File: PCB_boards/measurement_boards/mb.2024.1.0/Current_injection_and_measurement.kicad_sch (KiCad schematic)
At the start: 28 parts, among them J12 Conn_01x08_Socket, J14 Conn_01x02_Socket, J15 Conn_01x08_Socket, J20 shunt +, J21 shunt -, K3 G5LE-1, K4 G5LE-1, K5 G5LE-1, K6 G5LE-1, K7 G5LE-1, Q3 ZVN4206ASTZ, Q4 ZVN4206ASTZ, Q5 ZVN4206ASTZ, Q6 ZVN4206ASTZ, Q7 ZVN4206ASTZ, U5 1085

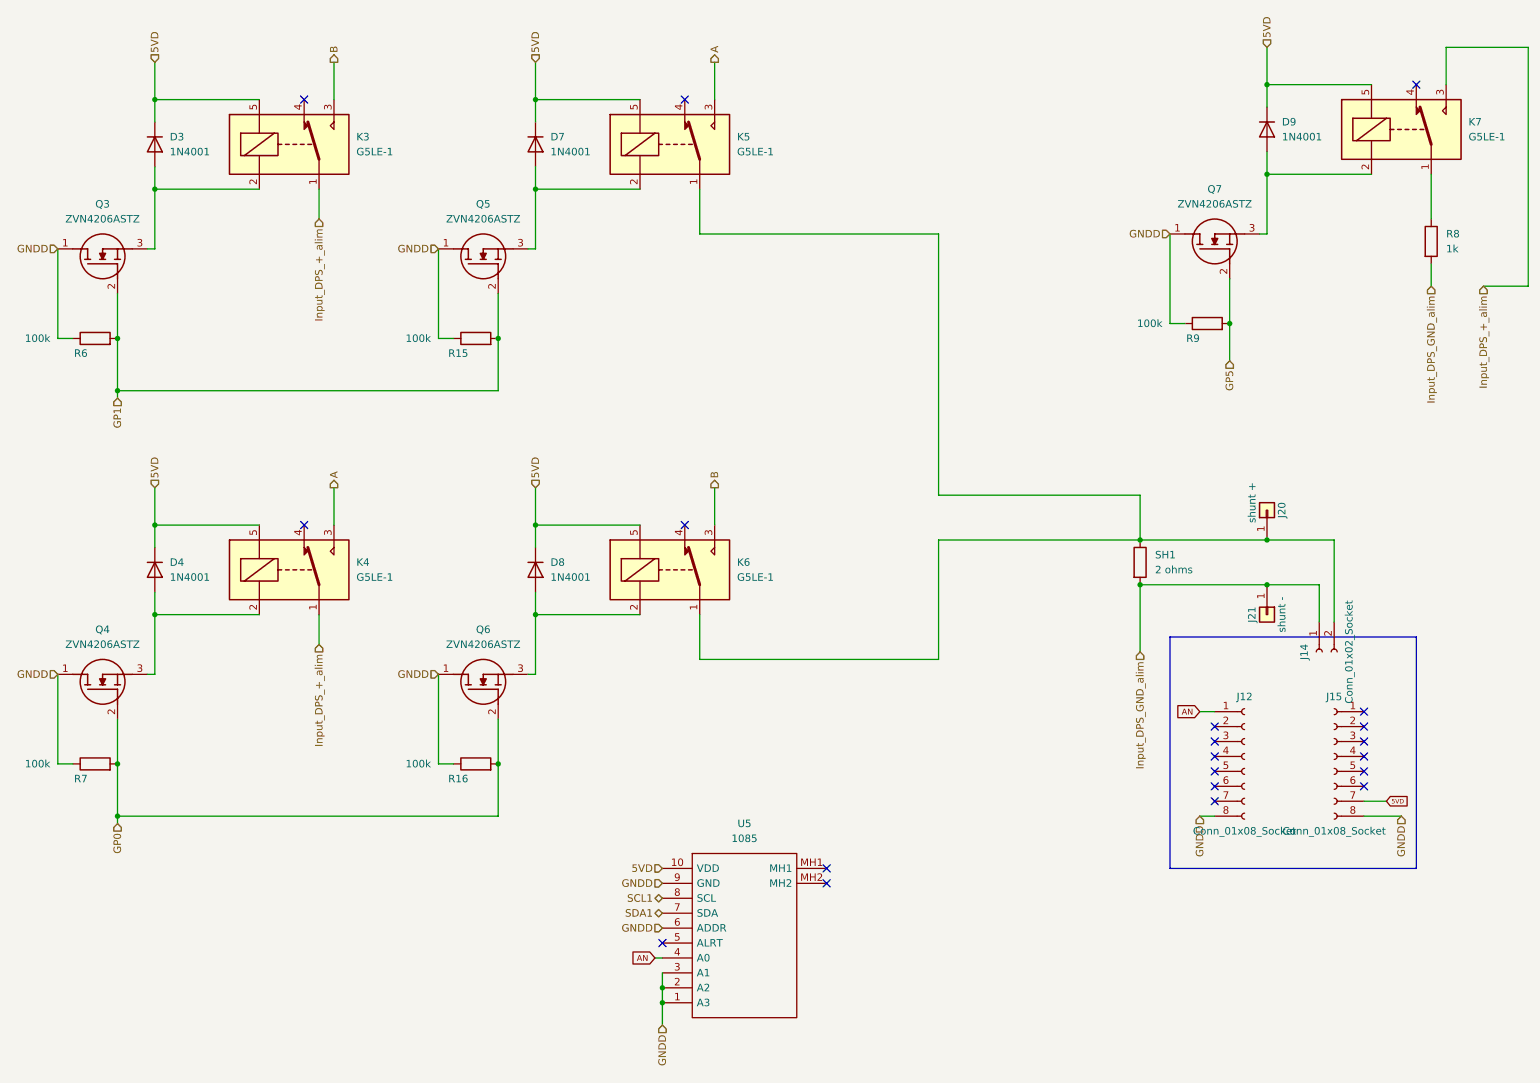
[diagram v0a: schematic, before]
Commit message: update diode 1n4007
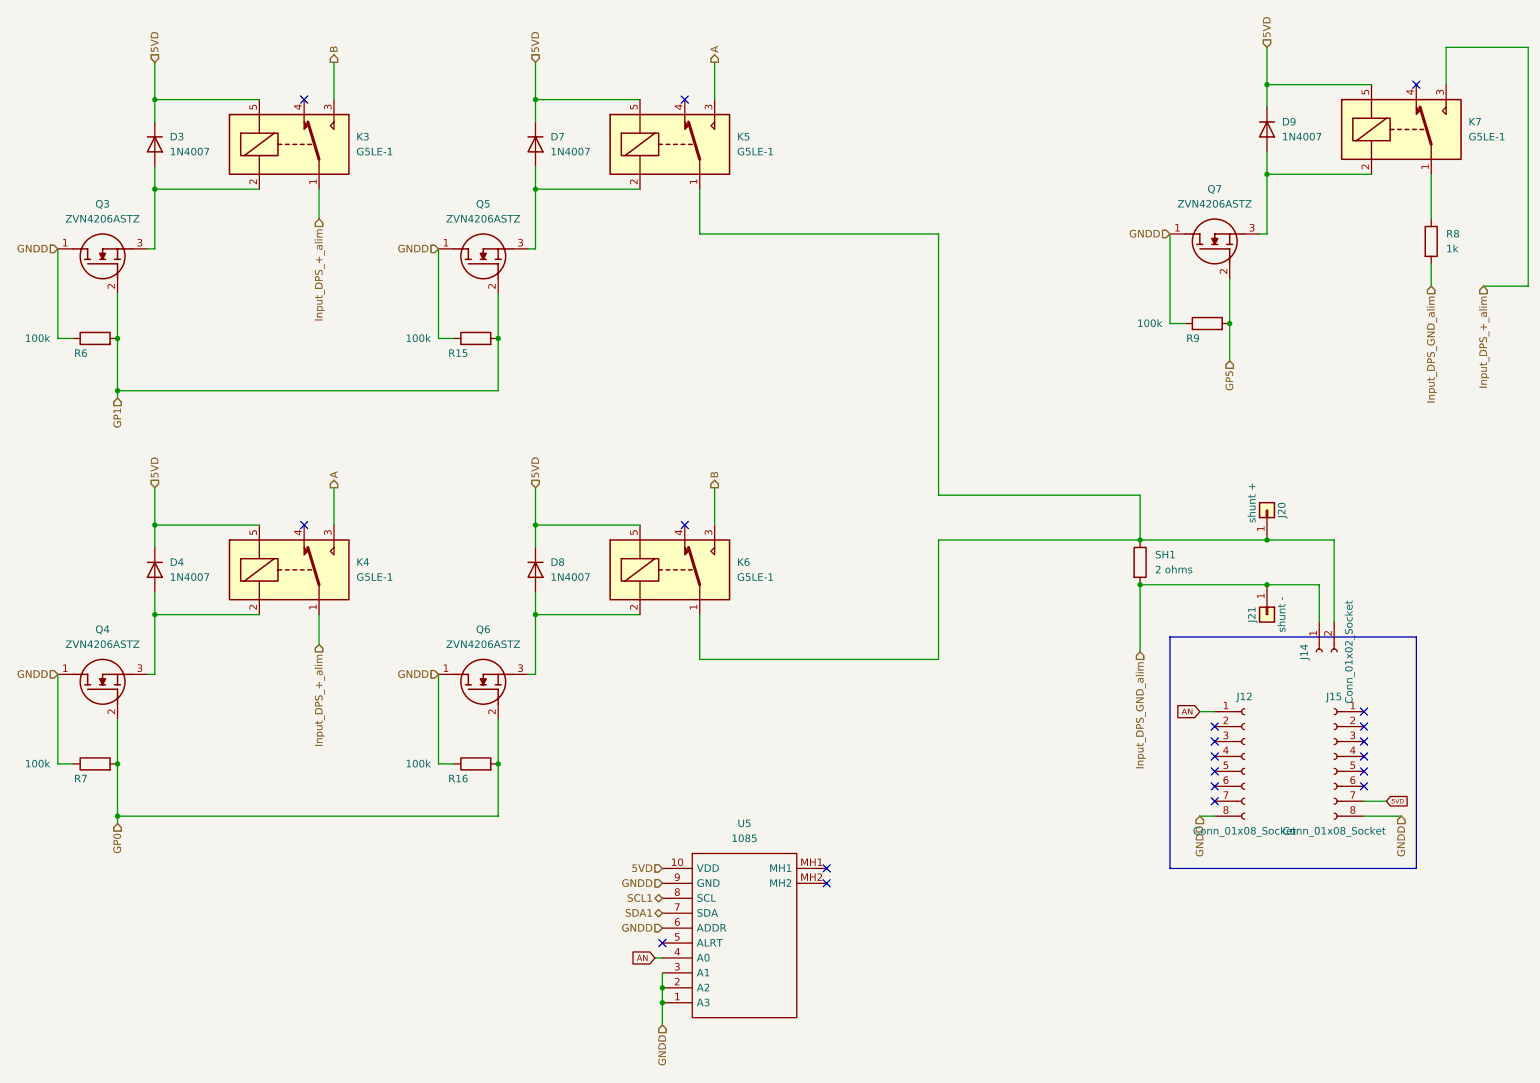
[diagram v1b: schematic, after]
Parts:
- D3, D4, D7, D8, D9: value 1N4001 -> 1N4007
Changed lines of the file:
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@@
     (pin "5")
     (instances
-      (project "mb.2024.0.3"
+      (project "mb.2024.1.0"
         (path "/62d2b953-c7cc-4d07-805d-38225011d95a/3a1d549c-401c-4ddf-9a51-4b7588f9097f"
           (reference "K6") (unit 1)
@@
       (effects (font (size 1.27 1.27)) (justify left))
     )
-    (property "Value" "1N4001" (at 49.53 36.83 90)
+    (property "Value" "1N4007" (at 49.53 36.83 90)
       (effects (font (size 1.27 1.27)) (justify left))
     )
@@
     (pin "2")
     (instances
-      (project "mb.2024.0.3"
+      (project "mb.2024.1.0"
         (path "/62d2b953-c7cc-4d07-805d-38225011d95a/3a1d549c-401c-4ddf-9a51-4b7588f9097f"
           (reference "D3") (unit 1)
@@
     (pin "5")
     (instances
-      (project "mb.2024.0.3"
+      (project "mb.2024.1.0"
         (path "/62d2b953-c7cc-4d07-805d-38225011d95a/3a1d549c-401c-4ddf-9a51-4b7588f9097f"
           (reference "K5") (unit 1)
@@
     (pin "5")
     (instances
-      (project "mb.2024.0.3"
+      (project "mb.2024.1.0"
         (path "/62d2b953-c7cc-4d07-805d-38225011d95a/3a1d549c-401c-4ddf-9a51-4b7588f9097f"
           (reference "K7") (unit 1)
@@
     (pin "3")
     (instances
-      (project "mb.2024.0.3"
+      (project "mb.2024.1.0"
         (path "/62d2b953-c7cc-4d07-805d-38225011d95a/3a1d549c-401c-4ddf-9a51-4b7588f9097f"
           (reference "Q4") (unit 1)
@@
     (pin "2")
     (instances
-      (project "mb.2024.0.3"
+      (project "mb.2024.1.0"
         (path "/62d2b953-c7cc-4d07-805d-38225011d95a/3a1d549c-401c-4ddf-9a51-4b7588f9097f"
           (reference "R15") (unit 1)
@@
     (pin "2")
     (instances
-      (project "mb.2024.0.3"
+      (project "mb.2024.1.0"
         (path "/62d2b953-c7cc-4d07-805d-38225011d95a/3a1d549c-401c-4ddf-9a51-4b7588f9097f"
           (reference "R6") (unit 1)
@@
     (pin "2")
     (instances
-      (project "mb.2024.0.3"
+      (project "mb.2024.1.0"
         (path "/62d2b953-c7cc-4d07-805d-38225011d95a/3a1d549c-401c-4ddf-9a51-4b7588f9097f"
           (reference "R16") (unit 1)
@@
     (pin "3")
     (instances
-      (project "mb.2024.0.3"
+      (project "mb.2024.1.0"
         (path "/62d2b953-c7cc-4d07-805d-38225011d95a/3a1d549c-401c-4ddf-9a51-4b7588f9097f"
           (reference "Q6") (unit 1)
@@
     (pin "3")
     (instances
-      (project "mb.2024.0.3"
+      (project "mb.2024.1.0"
         (path "/62d2b953-c7cc-4d07-805d-38225011d95a/3a1d549c-401c-4ddf-9a51-4b7588f9097f"
           (reference "Q3") (unit 1)
@@
     (pin "1")
     (instances
-      (project "mb.2024.0.3"
+      (project "mb.2024.1.0"
         (path "/62d2b953-c7cc-4d07-805d-38225011d95a/3a1d549c-401c-4ddf-9a51-4b7588f9097f"
           (reference "J20") (unit 1)
@@
     (pin "2")
     (instances
-      (project "mb.2024.0.3"
+      (project "mb.2024.1.0"
         (path "/62d2b953-c7cc-4d07-805d-38225011d95a/3a1d549c-401c-4ddf-9a51-4b7588f9097f"
           (reference "J14") (unit 1)
@@
       (effects (font (size 1.27 1.27)) (justify left))
     )
-    (property "Value" "1N4001" (at 114.3 109.22 90)
+    (property "Value" "1N4007" (at 114.3 109.22 90)
       (effects (font (size 1.27 1.27)) (justify left))
     )
@@
     (pin "2")
     (instances
-      (project "mb.2024.0.3"
+      (project "mb.2024.1.0"
         (path "/62d2b953-c7cc-4d07-805d-38225011d95a/3a1d549c-401c-4ddf-9a51-4b7588f9097f"
           (reference "D8") (unit 1)
@@
     (pin "1")
     (instances
-      (project "mb.2024.0.3"
+      (project "mb.2024.1.0"
         (path "/62d2b953-c7cc-4d07-805d-38225011d95a/3a1d549c-401c-4ddf-9a51-4b7588f9097f"
           (reference "J21") (unit 1)
@@
     (pin "8")
     (instances
-      (project "mb.2024.0.3"
+      (project "mb.2024.1.0"
         (path "/62d2b953-c7cc-4d07-805d-38225011d95a/3a1d549c-401c-4ddf-9a51-4b7588f9097f"
           (reference "J15") (unit 1)
@@
     (pin "3")
     (instances
-      (project "mb.2024.0.3"
+      (project "mb.2024.1.0"
         (path "/62d2b953-c7cc-4d07-805d-38225011d95a/3a1d549c-401c-4ddf-9a51-4b7588f9097f"
           (reference "Q7") (unit 1)
@@
       (effects (font (size 1.27 1.27)) (justify left))
     )
-    (property "Value" "1N4001" (at 238.76 34.29 90)
+    (property "Value" "1N4007" (at 238.76 34.29 90)
       (effects (font (size 1.27 1.27)) (justify left))
     )
@@
     (pin "2")
     (instances
-      (project "mb.2024.0.3"
+      (project "mb.2024.1.0"
         (path "/62d2b953-c7cc-4d07-805d-38225011d95a/3a1d549c-401c-4ddf-9a51-4b7588f9097f"
           (reference "D9") (unit 1)
@@
     (pin "2")
     (instances
-      (project "mb.2024.0.3"
+      (project "mb.2024.1.0"
         (path "/62d2b953-c7cc-4d07-805d-38225011d95a/3a1d549c-401c-4ddf-9a51-4b7588f9097f"
           (reference "R7") (unit 1)
@@
     (pin "2")
     (instances
-      (project "mb.2024.0.3"
+      (project "mb.2024.1.0"
         (path "/62d2b953-c7cc-4d07-805d-38225011d95a/3a1d549c-401c-4ddf-9a51-4b7588f9097f"
           (reference "R9") (unit 1)
@@
       (effects (font (size 1.27 1.27)) (justify left))
     )
-    (property "Value" "1N4001" (at 49.53 109.22 90)
+    (property "Value" "1N4007" (at 49.53 109.22 90)
       (effects (font (size 1.27 1.27)) (justify left))
     )
@@
     (pin "2")
     (instances
-      (project "mb.2024.0.3"
+      (project "mb.2024.1.0"
         (path "/62d2b953-c7cc-4d07-805d-38225011d95a/3a1d549c-401c-4ddf-9a51-4b7588f9097f"
           (reference "D4") (unit 1)
@@
     (pin "5")
     (instances
-      (project "mb.2024.0.3"
+      (project "mb.2024.1.0"
         (path "/62d2b953-c7cc-4d07-805d-38225011d95a/3a1d549c-401c-4ddf-9a51-4b7588f9097f"
           (reference "K3") (unit 1)
@@
     (pin "MH2")
     (instances
-      (project "mb.2024.0.3"
+      (project "mb.2024.1.0"
         (path "/62d2b953-c7cc-4d07-805d-38225011d95a/3a1d549c-401c-4ddf-9a51-4b7588f9097f"
           (reference "U5") (unit 1)
@@
     (pin "8")
     (instances
-      (project "mb.2024.0.3"
+      (project "mb.2024.1.0"
         (path "/62d2b953-c7cc-4d07-805d-38225011d95a/3a1d549c-401c-4ddf-9a51-4b7588f9097f"
           (reference "J12") (unit 1)
@@
     (pin "2")
     (instances
-      (project "mb.2024.0.3"
+      (project "mb.2024.1.0"
         (path "/62d2b953-c7cc-4d07-805d-38225011d95a/3a1d549c-401c-4ddf-9a51-4b7588f9097f"
           (reference "R8") (unit 1)
@@
       (effects (font (size 1.27 1.27)) (justify left))
     )
-    (property "Value" "1N4001" (at 114.3 36.83 90)
+    (property "Value" "1N4007" (at 114.3 36.83 90)
       (effects (font (size 1.27 1.27)) (justify left))
     )
@@
     (pin "2")
     (instances
-      (project "mb.2024.0.3"
+      (project "mb.2024.1.0"
         (path "/62d2b953-c7cc-4d07-805d-38225011d95a/3a1d549c-401c-4ddf-9a51-4b7588f9097f"
           (reference "D7") (unit 1)
@@
     (pin "5")
     (instances
-      (project "mb.2024.0.3"
+      (project "mb.2024.1.0"
         (path "/62d2b953-c7cc-4d07-805d-38225011d95a/3a1d549c-401c-4ddf-9a51-4b7588f9097f"
           (reference "K4") (unit 1)
@@
     (pin "2")
     (instances
-      (project "mb.2024.0.3"
+      (project "mb.2024.1.0"
         (path "/62d2b953-c7cc-4d07-805d-38225011d95a/3a1d549c-401c-4ddf-9a51-4b7588f9097f"
           (reference "SH1") (unit 1)
@@
     (pin "3")
     (instances
-      (project "mb.2024.0.3"
+      (project "mb.2024.1.0"
         (path "/62d2b953-c7cc-4d07-805d-38225011d95a/3a1d549c-401c-4ddf-9a51-4b7588f9097f"
           (reference "Q5") (unit 1)
